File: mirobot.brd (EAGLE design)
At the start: 55.6 x 39 mm, 13 parts, among them X1 5_PIN_STEPPER, X2 5_PIN_STEPPER

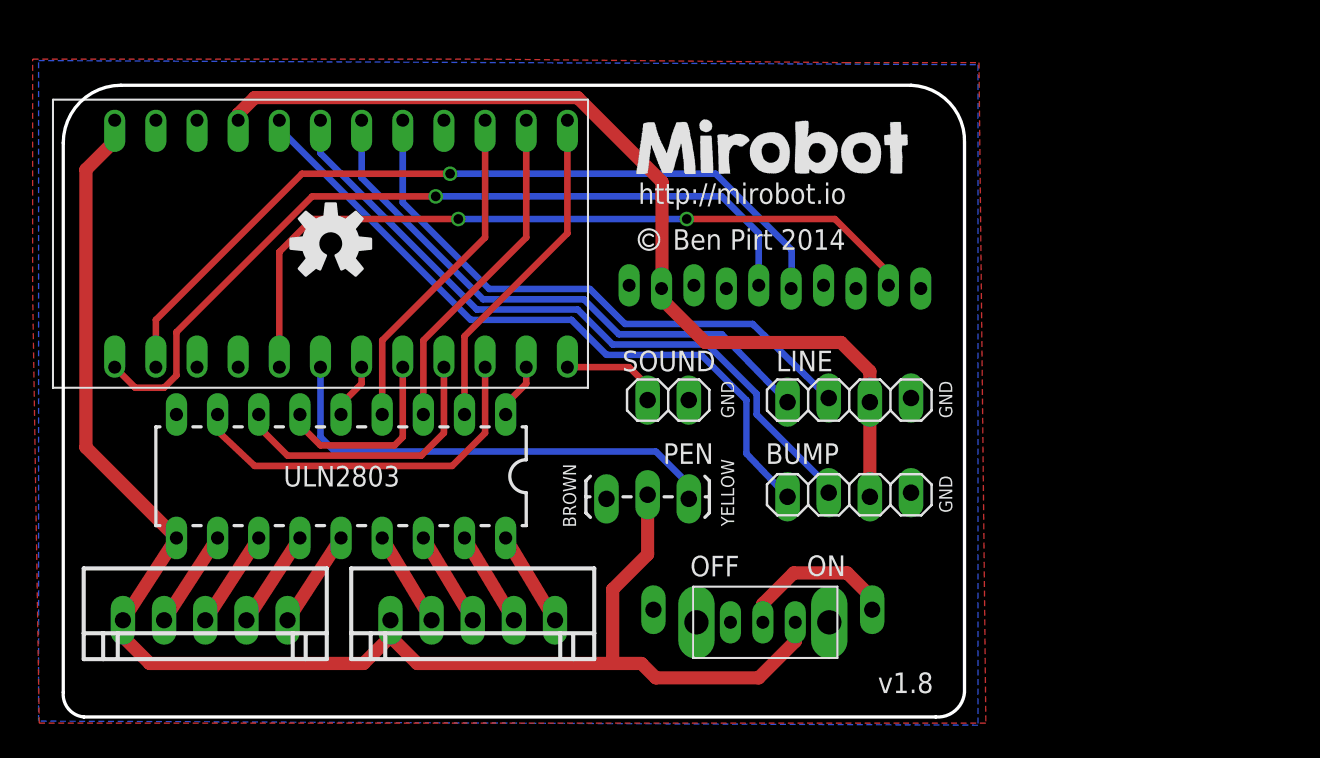
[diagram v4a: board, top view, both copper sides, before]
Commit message: Updated to make switch easier to reach
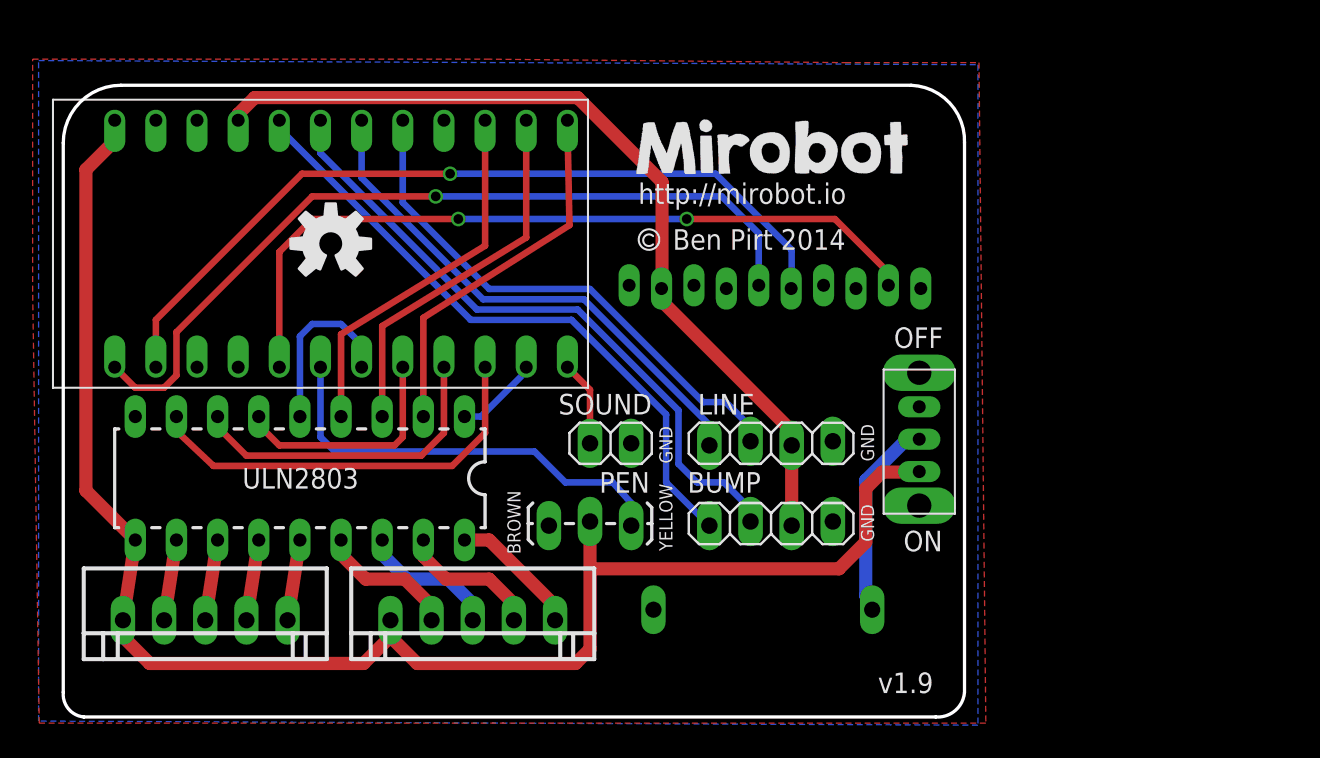
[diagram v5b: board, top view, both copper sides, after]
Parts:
- moved U$3 14.9 mm to (61.7, 32.9), turned to 270 degrees
- moved LINE 5.51 mm to (52.6, 32.6)
- moved BUMP 5.14 mm to (52.6, 27.7)
- moved SOUND 4.45 mm to (42.7, 32.6)
- moved PEN 3.92 mm to (43.9, 27.6)
- moved ULN2803 2.54 mm to (23.5, 30.5)
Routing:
- net MOTOR2_1: track 3.45 -> 11.0 mm
- net +3V3: track 58.8 -> 53.7 mm
- net VSS: track 94.4 -> 98.8 mm
- net PC3: track 43.3 -> 39.7 mm
- net PC0: track 36.3 -> 33.2 mm
- net PC1: track 35.6 -> 32.6 mm
- net N$2: track 5.92 -> 8.83 mm
- net N$3: track 5.92 -> 8.76 mm
- net N$4: track 5.92 -> 8.68 mm
- net PC2: track 43.1 -> 40.4 mm
- net SERVO: track 29.1 -> 26.6 mm
- net N$6: track 10.0 -> 12.5 mm
- net MOTOR1_3: track 20.8 -> 23.3 mm
- net MOTOR1_4: track 20.8 -> 23.3 mm
- net MOTOR1_2: track 20.8 -> 23.2 mm
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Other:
- board text added: "v1.9"
- board text removed: "v1.8"

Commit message: Updated outlines slightly
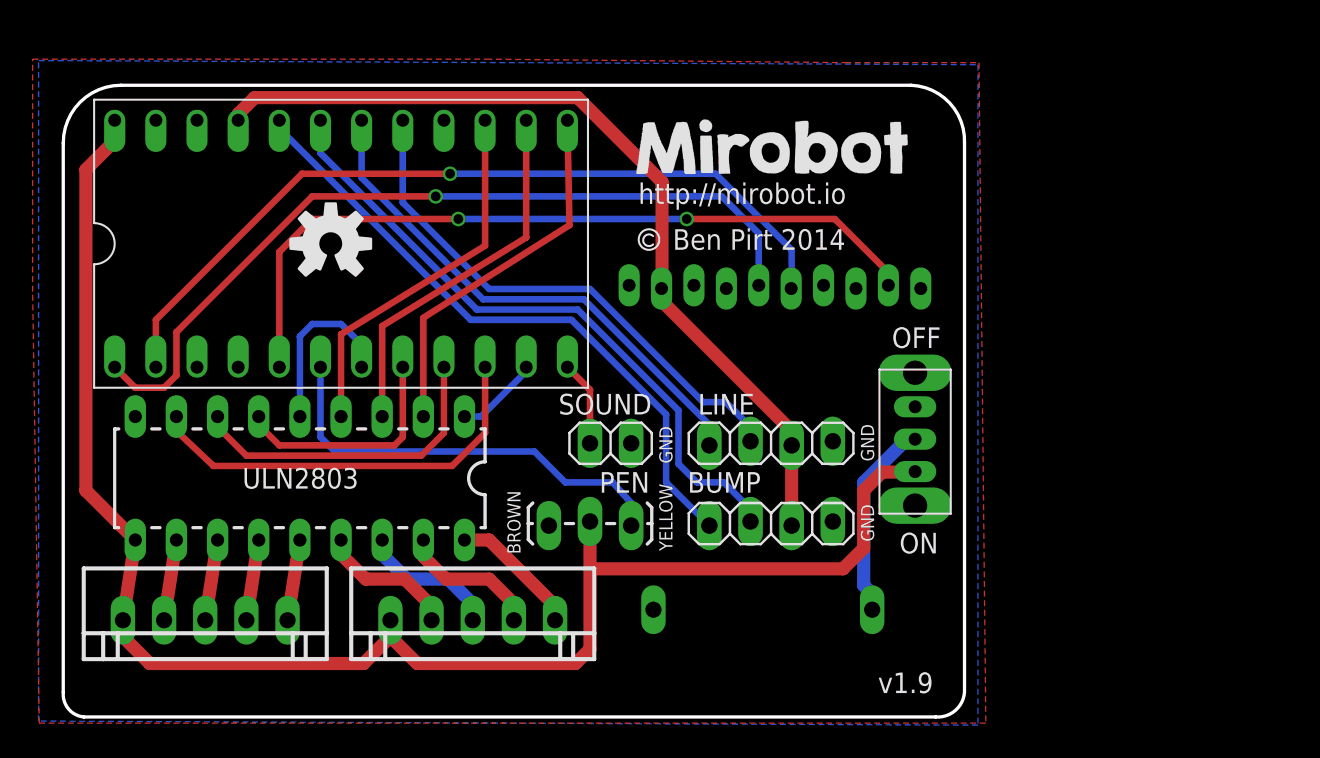
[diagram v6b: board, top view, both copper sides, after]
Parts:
- moved U$3 0.25 mm to (61.5, 32.9)
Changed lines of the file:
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@@
 <wire x1="61.214" y1="54.737" x2="12.446" y2="54.737" width="0.2032" layer="20"/>
 <wire x1="12.446" y1="54.737" x2="8.89" y2="51.181" width="0.2032" layer="20" curve="90"/>
-<text x="60.7481125" y="25.971425" size="1.27" layer="21" ratio="10">ON</text>
-<text x="60.15558125" y="38.523265625" size="1.27" layer="21" ratio="10">OFF</text>
+<text x="60.4941125" y="25.844425" size="1.27" layer="21" ratio="10">ON</text>
+<text x="60.02858125" y="38.523265625" size="1.27" layer="21" ratio="10">OFF</text>
 <text x="44.381496875" y="47.41603125" size="1.27" layer="21" ratio="10">http://mirobot.io</text>
 <text x="58.123584375" y="33.824165625" size="0.8128" layer="25" rot="R270">GND</text>
@@
 <element name="U$1" library="usr_wifi" package="WIFI_MODULE-T" value="USR_WIFI-T" x="51.816" y="42.291"/>
 <element name="U$2" library="custom" package="ARDUINO_PRO_MINI" value="ARDUINO_PRO_MINI" x="24.765" y="44.958" rot="R90"/>
-<element name="U$3" library="custom" package="SPDT_SLIDE_SWITCH" value="SPDT_SLIDE_SWITCH" x="61.722" y="32.893" rot="R270"/>
+<element name="U$3" library="custom" package="SPDT_SLIDE_SWITCH" value="SPDT_SLIDE_SWITCH" x="61.468" y="32.893" rot="R270"/>
 <element name="ULN2803" library="SparkFun-PowerIC" package="DIL18" value="" x="23.495" y="30.48" smashed="yes" rot="R180">
 <attribute name="NAME" x="19.939" y="29.845" size="1.27" layer="25" ratio="10"/>
@@
 <wire x1="29.083" y1="20.701" x2="29.083" y2="21.717" width="0.8128" layer="1"/>
 <wire x1="41.402" y1="27.813" x2="41.402" y2="24.892" width="0.8128" layer="1"/>
-<wire x1="41.402" y1="24.892" x2="56.769" y2="24.892" width="0.8128" layer="1"/>
-<wire x1="56.769" y1="24.892" x2="58.42" y2="26.543" width="0.8128" layer="1"/>
-<wire x1="58.42" y1="26.543" x2="58.42" y2="29.845" width="0.8128" layer="1"/>
-<wire x1="58.42" y1="29.845" x2="59.436" y2="30.861" width="0.8128" layer="1"/>
+<wire x1="41.402" y1="24.892" x2="57.023" y2="24.892" width="0.8128" layer="1"/>
+<wire x1="57.023" y1="24.892" x2="58.293" y2="26.162" width="0.8128" layer="1"/>
+<wire x1="58.293" y1="26.162" x2="58.293" y2="29.718" width="0.8128" layer="1"/>
+<wire x1="58.293" y1="29.718" x2="59.436" y2="30.861" width="0.8128" layer="1"/>
 <wire x1="59.436" y1="30.861" x2="61.69" y2="30.861" width="0.8128" layer="1"/>
-<wire x1="61.69" y1="30.861" x2="61.722" y2="30.893" width="0.8128" layer="1"/>
+<wire x1="61.69" y1="30.861" x2="61.468" y2="30.893" width="0.8128" layer="1"/>
 </signal>
 <signal name="+3V3">
@@
 <contactref element="U$3" pad="COMMON"/>
 <contactref element="U$4" pad="VSS"/>
-<wire x1="61.722" y1="32.893" x2="60.96" y2="32.893" width="0.8128" layer="16"/>
-<wire x1="60.96" y1="32.893" x2="58.42" y2="30.353" width="0.8128" layer="16"/>
-<wire x1="58.42" y1="30.353" x2="58.42" y2="23.241" width="0.8128" layer="16"/>
-<wire x1="58.42" y1="23.241" x2="58.801" y2="22.86" width="0.8128" layer="16"/>
-<wire x1="58.801" y1="22.86" x2="58.801" y2="22.384" width="0.8128" layer="16"/>
+<wire x1="61.468" y1="32.893" x2="60.96" y2="32.893" width="0.8128" layer="16"/>
+<wire x1="60.96" y1="32.893" x2="58.293" y2="30.226" width="0.8128" layer="16"/>
+<wire x1="58.293" y1="30.226" x2="58.293" y2="23.876" width="0.8128" layer="16"/>
+<wire x1="58.293" y1="23.876" x2="58.801" y2="23.368" width="0.8128" layer="16"/>
+<wire x1="58.801" y1="23.368" x2="58.801" y2="22.384" width="0.8128" layer="16"/>
 <wire x1="58.801" y1="22.384" x2="58.817" y2="22.368" width="0.8128" layer="16"/>
 </signal>

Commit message: v1.9 board
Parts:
- moved LOGO1 0.80 mm to (26.2, 44.7)
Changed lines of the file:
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@@
 </element>
 <element name="U$4" library="custom" package="BATTERY_PACK" value="BATTERY_PACK" x="59.817" y="23.368" rot="MR180"/>
-<element name="LOGO1" library="SparkFun-Aesthetics" package="OSHW-LOGO-M" value="OSHW-LOGOM" x="25.4" y="44.958"/>
+<element name="LOGO1" library="SparkFun-Aesthetics" package="OSHW-LOGO-M" value="OSHW-LOGOM" x="26.162" y="44.704"/>
 <element name="U$5" library="custom" package="LOGO" value="" x="52.533553125" y="50.729796875"/>
 <element name="LINE" library="Child-Friendly-Parts" package="1X04" value="" x="52.578" y="32.639" smashed="yes">
